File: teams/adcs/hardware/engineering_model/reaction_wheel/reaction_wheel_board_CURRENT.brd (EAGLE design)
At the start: 94 x 94 mm, 94 parts, among them U2 TPS732XX, U3 TPS732XX

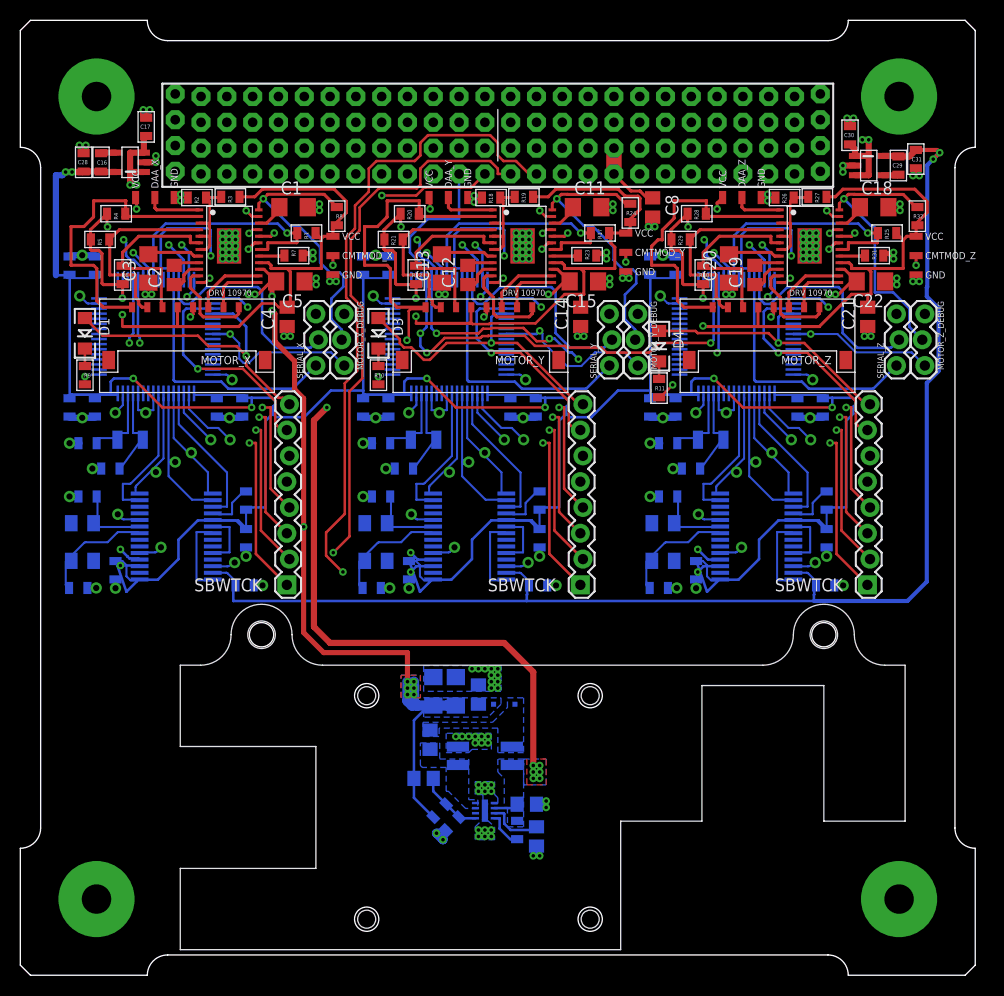
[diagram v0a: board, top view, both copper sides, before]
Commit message: ADCS/RW: Add new reaction wheel footprint to board
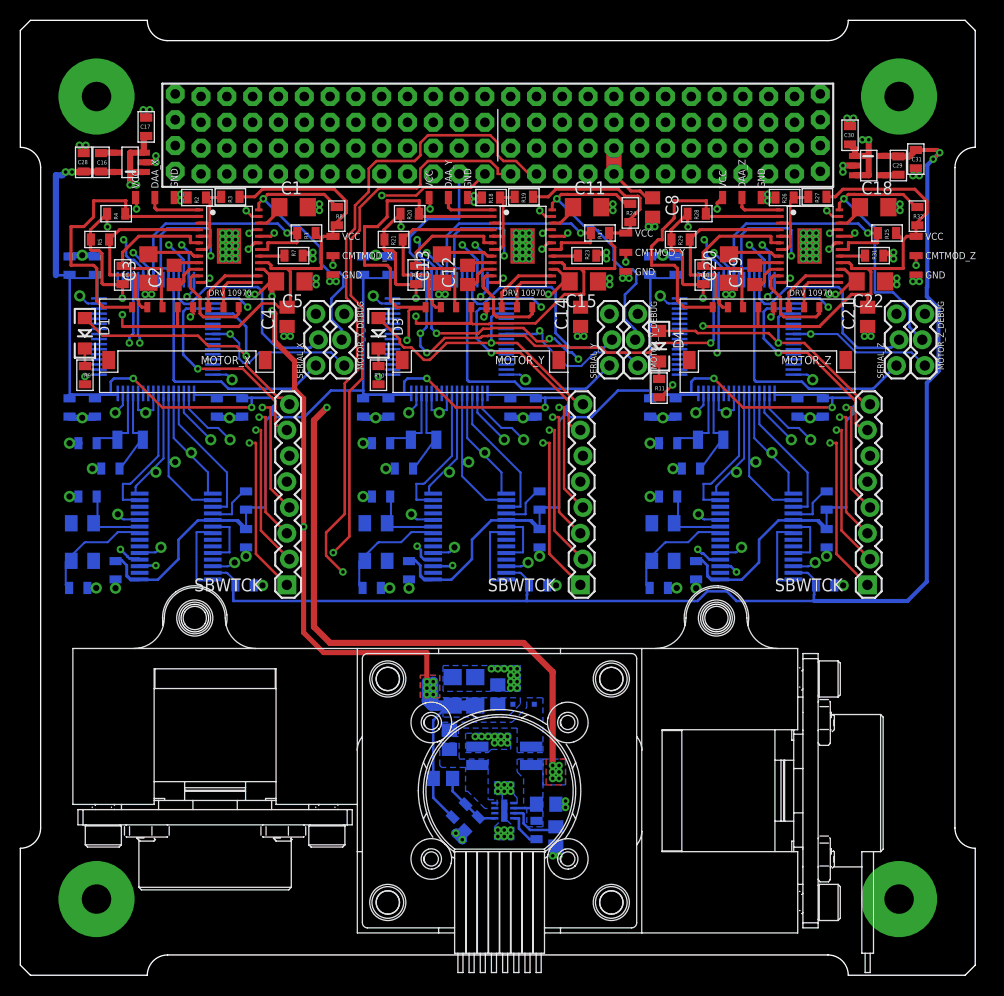
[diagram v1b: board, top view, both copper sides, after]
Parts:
- moved U$9 2.73 mm to (46.0, 16.8)
- moved C26 1.91 mm to (50.5, 15.6)
- moved C27 1.91 mm to (51.4, 12.4)
- moved C32 1.91 mm to (41.0, 21.9)
- moved C33 1.91 mm to (43.5, 26.7)
- moved C34 1.91 mm to (40.3, 18.1)
- moved C35 1.91 mm to (45.7, 26.4)
- moved C36 1.91 mm to (41.3, 26.7)
- moved D5 1.91 mm to (48.3, 25.4)
- moved R15 1.91 mm to (49.5, 13.0)
- moved R33 1.91 mm to (43.2, 13.7)
- moved L2 1.90 mm to (46.4, 20.3)
- moved R16 1.90 mm to (41.9, 14.9)
- moved U$6 1.90 mm to (46.4, 14.9)
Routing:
- net +3V3: track 246.9 -> 242.9 mm
- net VM: track 183.8 -> 185.7 mm
- net VBAT: track 178.8 -> 180.7 mm
- net +5V: track 124.3 -> 125.1 mm
- net CANH: track 120.6 -> 121.3 mm

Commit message: ADCS/RW: Clean up schematic
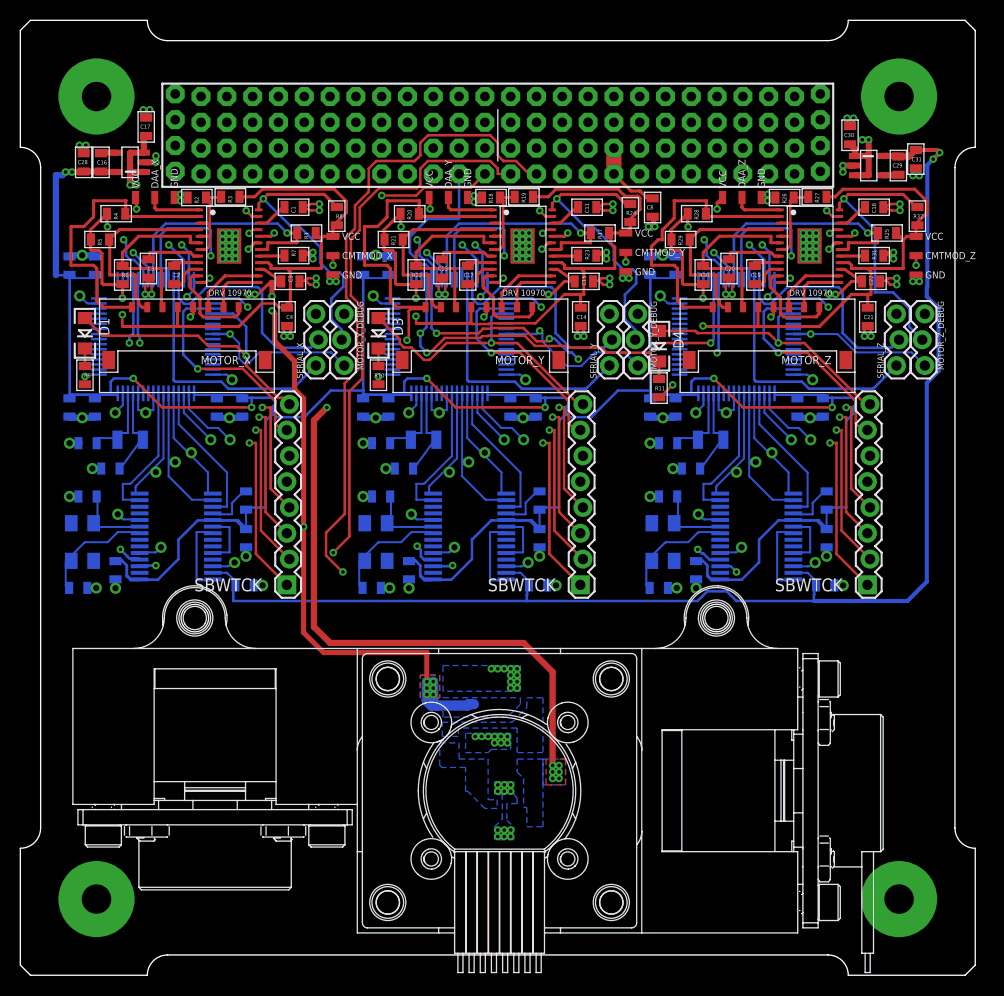
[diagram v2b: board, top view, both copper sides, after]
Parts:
- removed C26, C27: 2.2 μF, rcl:C0805
- removed C32: 1 μF, rcl:C0805
- removed C33: 22 μF, rcl:C1206
- removed C34: 5.6 pF, rcl:C0805
- removed C35: 10 μF, rcl:C0805
- removed C36: 47 μF, rcl:C1206
- removed D5: PMEG6010CEJ, DubSat1 Components:SC-90
- removed L2: WURTH_ELEKTRONIK_INDDD_744877001, DubSat1 Components:WURTH_ELEKTRONIK_INDDD_744877001
- removed R15: 1 kΩ, DubSat1 Components:0805
- removed R16: 330 kΩ, DubSat1 Components:0805
- removed R33: 120 kΩ, DubSat1 Components:0805
- removed U$6: LT8335, DubSat1 Components:DDB
- C1, C11, C13, C15, C18, C20, C22, C3, C5: device rcl:C1206 -> DubSat1 Components:0805
- C12, C14, C19, C2, C21, C4: device rcl:C0805 -> DubSat1 Components:0805
- C16, C29: value 0.01 μF -> 0.01uF
- C17, C28, C30: value 1 μF -> 1uF
- C31: value 1μF -> 1uF
- C8: value 10 uF -> 10uF; device rcl:C0805 -> DubSat1 Components:0805
- R1, R17, R18, R19, R2, R24, R25, R26, R27, R3, R32, R8: value 3.3K -> 3.3k
- R10, R11, R9: value (none) -> 330
- R20, R21, R22, R28, R29, R30, R4, R5, R6: value 10K -> 10k
- R23, R31, R7: value (none) -> 273k
- U2, U3: value TPS732XX -> LT1761-X
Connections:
- removed net EN_UVLO: R15.2, U$6.P$8
- removed net FBX: C34.2, R16.1, R33.2, U$6.P$1
- removed net INT_VCC: C27.1, U$6.P$7
- removed net SW: C32.1, L2.P$3, U$6.P$3, U$6.P$4
- removed net VD: C32.2, D5.P$1, L2.P$1
- removed net VM: C15.2, C22.2, C33.1, C34.1, C35.1, C36.1, C5.2, D5.P$2, R16.2, U$12.VM, U$15.VM, U$7.VM
- net GND: no longer C26.2, C27.2, C33.2, C35.2, C36.2, L2.P$2, R33.1, U$6.GND, U$6.P$5
- net VBAT: now also C15.2, C22.2, C5.2, U$12.VM, U$15.VM, U$7.VM; no longer C26.1, L2.P$4, R15.1, U$6.P$6
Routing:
- net VM: track 185.7 -> 0.00 mm, vias 14 -> 0
- net VBAT: track 180.7 -> 354.1 mm, vias 11 -> 25
- net FBX: track 6.52 -> 0.00 mm
- net INT_VCC: track 5.53 -> 0.00 mm
- net EN_UVLO: track 3.70 -> 0.00 mm
- net GND: track 119.2 -> 119.0 mm, vias 148 -> 142
- removed copper zone on layer 1, net VM
- removed copper zone on layer 16, net VM

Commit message: ADCS/RW: Update LDO capacitor values
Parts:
- C28, C31: value 1uF -> 10uF
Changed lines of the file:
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@@
 <element name="C16" library="DubSat1 Components" package="0805" value="0.01uF" x="6.6675" y="78.74" rot="R90"/>
 <element name="C17" library="DubSat1 Components" package="0805" value="1uF" x="11.1125" y="82.2325" rot="R270"/>
-<element name="C28" library="DubSat1 Components" package="0805" value="1uF" x="4.953" y="78.74" rot="R270"/>
+<element name="C28" library="DubSat1 Components" package="0805" value="10uF" x="4.953" y="78.74" rot="R270"/>
 <element name="U3" library="DubSat1 Components" package="SOT-23-5" value="LT1761-X" x="82.2325" y="78.4225" rot="R270"/>
 <element name="C29" library="DubSat1 Components" package="0805" value="0.01uF" x="85.1535" y="78.4225" rot="R270"/>
 <element name="C30" library="DubSat1 Components" package="0805" value="1uF" x="80.391" y="81.407" rot="R270"/>
-<element name="C31" library="DubSat1 Components" package="0805" value="1uF" x="86.868" y="79.0575" rot="R90"/>
+<element name="C31" library="DubSat1 Components" package="0805" value="10uF" x="86.868" y="79.0575" rot="R90"/>
 <element name="D1" library="DubSat1 Components" package="LED-1206" value="" x="5.08" y="61.9125" rot="R270"/>
 <element name="D3" library="DubSat1 Components" package="LED-1206" value="" x="33.9725" y="61.9125" rot="R270"/>
